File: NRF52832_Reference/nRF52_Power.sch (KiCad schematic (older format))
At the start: 32 parts

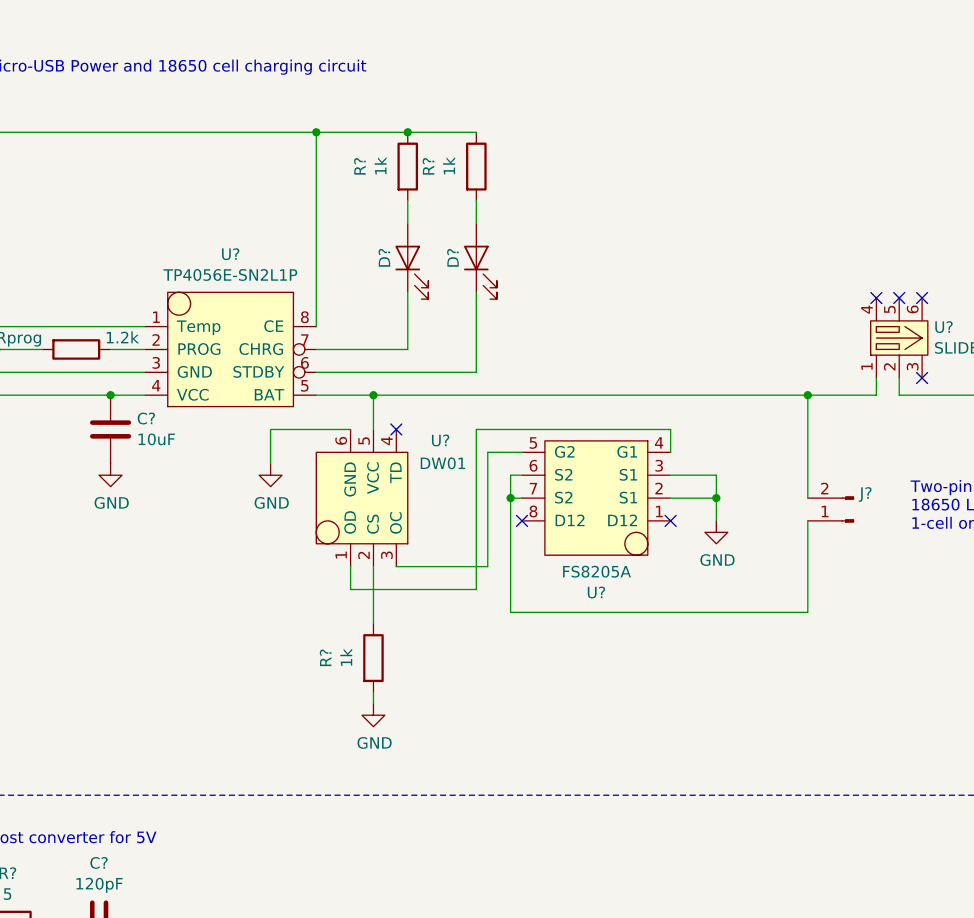
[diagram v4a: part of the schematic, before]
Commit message: Set footprints for some components of battery charging circuit.
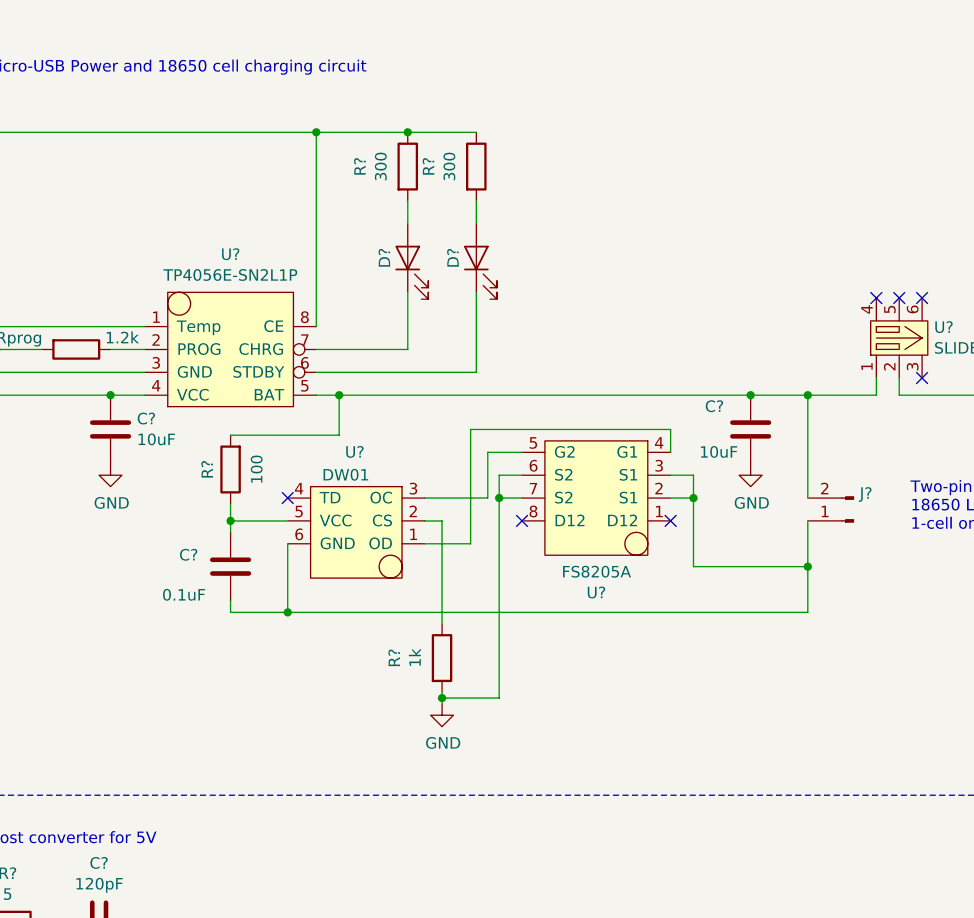
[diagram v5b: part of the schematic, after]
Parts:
- added C?: 10uF, Capacitor_SMD:C_0603_1608Metric_Pad1.05x0.95mm_HandSolder, symbol Device:C
- added C?: 0.1uF, Capacitor_SMD:C_0603_1608Metric_Pad1.05x0.95mm_HandSolder, symbol Device:C
- added R?: 100, Resistor_SMD:R_0603_1608Metric_Pad1.05x0.95mm_HandSolder, symbol Device:R
- C?: footprint (none) -> Capacitor_SMD:C_0603_1608Metric_Pad1.05x0.95mm_HandSolder
- D? (x2): footprint (none) -> LED_SMD:LED_0603_1608Metric_Pad1.05x0.95mm_HandSolder
- R? (x2): value 1k -> 300; footprint (none) -> Resistor_SMD:R_0603_1608Metric_Pad1.05x0.95mm_HandSolder
- R? (x5), Rprog: footprint (none) -> Resistor_SMD:R_0603_1608Metric_Pad1.05x0.95mm_HandSolder
- U?: footprint (none) -> Package_SO:SOIC-8-1EP_3.9x4.9mm_P1.27mm_EP2.35x2.35mm
- U?: footprint (none) -> Package_TO_SOT_SMD:SOT-23-6_Handsoldering
- U?: footprint (none) -> Package_SO:TSSOP-8_4.4x3mm_P0.65mm
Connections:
- net GND: now also U?.6 (S2), U?.7 (S2), C?.2; no longer U?.2 (S1), U?.3 (S1), U?.6 (GND)
- net at J?.2 (Pin_2), U?.1, U?.5 (BAT): now also C?.1, R?.2; no longer U?.5 (VCC)
- new net: C?.2, J?.1 (Pin_1), U?.2 (S1), U?.3 (S1), U?.6 (GND)
- new net: C?.1, R?.1, U?.5 (VCC)
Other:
- moved on the sheet: R?, U?
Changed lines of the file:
@@
 F 0 "D?" H 3850 1650 50  0000 C CNN
 F 1 "LED" H 3841 1675 50  0001 C CNN
-F 2 "" H 3850 1550 50  0001 C CNN
+F 2 "LED_SMD:LED_0603_1608Metric_Pad1.05x0.95mm_HandSolder" H 3850 1550 50  0001 C CNN
 F 3 "~" H 3850 1550 50  0001 C CNN
 	1    3850 1550
@@
 F 0 "D?" H 3550 1650 50  0000 C CNN
 F 1 "LED" H 3541 1675 50  0001 C CNN
-F 2 "" H 3550 1550 50  0001 C CNN
+F 2 "LED_SMD:LED_0603_1608Metric_Pad1.05x0.95mm_HandSolder" H 3550 1550 50  0001 C CNN
 F 3 "~" H 3550 1550 50  0001 C CNN
 	1    3550 1550
@@
 P 3850 1150
 F 0 "R?" V 3643 1150 50  0000 C CNN
-F 1 "1k" V 3734 1150 50  0000 C CNN
-F 2 "" V 3780 1150 50  0001 C CNN
+F 1 "300" V 3734 1150 50  0000 C CNN
+F 2 "Resistor_SMD:R_0603_1608Metric_Pad1.05x0.95mm_HandSolder" V 3780 1150 50  0001 C CNN
 F 3 "~" H 3850 1150 50  0001 C CNN
 	1    3850 1150
@@
 P 3550 1150
 F 0 "R?" V 3343 1150 50  0000 C CNN
-F 1 "1k" V 3434 1150 50  0000 C CNN
-F 2 "" V 3480 1150 50  0001 C CNN
+F 1 "300" V 3434 1150 50  0000 C CNN
+F 2 "Resistor_SMD:R_0603_1608Metric_Pad1.05x0.95mm_HandSolder" V 3480 1150 50  0001 C CNN
 F 3 "~" H 3550 1150 50  0001 C CNN
 	1    3550 1150
@@
 F 0 "U?" H 2775 2365 50  0000 C CNN
 F 1 "TP4056E-SN2L1P" H 2775 2274 50  0000 C CNN
-F 2 "" H 2650 1950 50  0001 C CNN
+F 2 "Package_SO:SOIC-8-1EP_3.9x4.9mm_P1.27mm_EP2.35x2.35mm" H 2650 1950 50  0001 C CNN
 F 3 "" H 2650 1950 50  0001 C CNN
 	1    2650 1950
 	1    0    0    -1
-$EndComp
-$Comp
-L Project_Libary:DW01 U?
-U 1 1 5BF3803F
-P 3450 2650
-F 0 "U?" V 3750 2450 50  0000 R CNN
-F 1 "DW01" V 3650 2500 50  0000 R CNN
-F 2 "" H 3450 2650 50  0001 C CNN
-F 3 "" H 3450 2650 50  0001 C CNN
-	1    3450 2650
-	0    -1   -1   0
 $EndComp
 $Comp
@@
 F 0 "U?" H 4425 3015 50  0000 C CNN
 F 1 "FS8205A" H 4425 2924 50  0000 C CNN
-F 2 "" H 4450 2950 50  0001 C CNN
+F 2 "Package_SO:TSSOP-8_4.4x3mm_P0.65mm" H 4450 2950 50  0001 C CNN
 F 3 "" H 4450 2950 50  0001 C CNN
 	1    4400 2650
@@
 F 0 "Rprog" V 2050 1700 50  0000 C CNN
 F 1 "1.2k" V 2050 2150 50  0000 C CNN
-F 2 "" V 2030 1950 50  0001 C CNN
+F 2 "Resistor_SMD:R_0603_1608Metric_Pad1.05x0.95mm_HandSolder" V 2030 1950 50  0001 C CNN
 F 3 "~" H 2100 1950 50  0001 C CNN
 	1    2100 1950
@@
 Wire Wire Line
 	3850 2050 3850 1700
-NoConn ~ 3500 2300
-Wire Wire Line
-	3400 2150 3400 2300
-$Comp
-L power:GND #PWR?
-U 1 1 5BF3E673
-P 2950 2450
-F 0 "#PWR?" H 2950 2200 50  0001 C CNN
-F 1 "GND" H 2955 2277 50  0000 C CNN
-F 2 "" H 2950 2450 50  0001 C CNN
-F 3 "" H 2950 2450 50  0001 C CNN
-	1    2950 2450
-	1    0    0    -1
-$EndComp
-Wire Wire Line
-	3300 2300 2950 2300
-Wire Wire Line
-	2950 2300 2950 2450
+NoConn ~ 3025 2600
 Wire Wire Line
 	1550 2150 1550 1000
@@
 F 0 "C?" H 2365 2346 50  0000 L CNN
 F 1 "10uF" H 2365 2255 50  0000 L CNN
-F 2 "" H 2288 2150 50  0001 C CNN
+F 2 "Capacitor_SMD:C_0603_1608Metric_Pad1.05x0.95mm_HandSolder" H 2288 2150 50  0001 C CNN
 F 3 "~" H 2250 2300 50  0001 C CNN
 	1    2250 2300
@@
 L Device:R R?
 U 1 1 5BF44C1F
-P 3400 3300
-F 0 "R?" V 3193 3300 50  0000 C CNN
-F 1 "1k" V 3284 3300 50  0000 C CNN
-F 2 "" V 3330 3300 50  0001 C CNN
-F 3 "~" H 3400 3300 50  0001 C CNN
-	1    3400 3300
+P 3700 3300
+F 0 "R?" V 3493 3300 50  0000 C CNN
+F 1 "1k" V 3584 3300 50  0000 C CNN
+F 2 "Resistor_SMD:R_0603_1608Metric_Pad1.05x0.95mm_HandSolder" V 3630 3300 50  0001 C CNN
+F 3 "~" H 3700 3300 50  0001 C CNN
+	1    3700 3300
 	1    0    0    -1
 $EndComp
@@
 L power:GND #PWR?
 U 1 1 5BF44FAE
-P 3400 3500
-F 0 "#PWR?" H 3400 3250 50  0001 C CNN
-F 1 "GND" H 3405 3327 50  0000 C CNN
-F 2 "" H 3400 3500 50  0001 C CNN
-F 3 "" H 3400 3500 50  0001 C CNN
-	1    3400 3500
-	1    0    0    -1
-$EndComp
-Wire Wire Line
-	3500 2900 3900 2900
-Wire Wire Line
-	3900 2900 3900 2400
+P 3700 3500
+F 0 "#PWR?" H 3700 3250 50  0001 C CNN
+F 1 "GND" H 3705 3327 50  0000 C CNN
+F 2 "" H 3700 3500 50  0001 C CNN
+F 3 "" H 3700 3500 50  0001 C CNN
+	1    3700 3500
+	1    0    0    -1
+$EndComp
 Wire Wire Line
 	3900 2400 4050 2400
 Wire Wire Line
-	3400 2900 3400 3150
-Wire Wire Line
-	3400 3450 3400 3500
-Wire Wire Line
-	3300 3000 3850 3000
-Wire Wire Line
-	3850 3000 3850 2300
-Wire Wire Line
-	3850 2300 4700 2300
-Wire Wire Line
 	4700 2300 4700 2400
-Wire Wire Line
-	3300 2900 3300 3000
 $Comp
 L power:GND #PWR?
 U 1 1 5BF49B8A
-P 4900 2700
-F 0 "#PWR?" H 4900 2450 50  0001 C CNN
-F 1 "GND" H 4905 2527 50  0000 C CNN
-F 2 "" H 4900 2700 50  0001 C CNN
-F 3 "" H 4900 2700 50  0001 C CNN
-	1    4900 2700
-	1    0    0    -1
-$EndComp
-Wire Wire Line
-	4700 2600 4900 2600
-Wire Wire Line
-	4900 2600 4900 2700
-Wire Wire Line
-	4700 2500 4900 2500
-Wire Wire Line
-	4900 2500 4900 2600
-Connection ~ 4900 2600
-Wire Wire Line
-	4050 2500 4000 2500
-Wire Wire Line
-	4000 2500 4000 2600
-Wire Wire Line
-	4000 3100 5300 3100
-Wire Wire Line
-	5300 3100 5300 2700
+P 5050 2450
+F 0 "#PWR?" H 5050 2200 50  0001 C CNN
+F 1 "GND" H 5055 2277 50  0000 C CNN
+F 2 "" H 5050 2450 50  0001 C CNN
+F 3 "" H 5050 2450 50  0001 C CNN
+	1    5050 2450
+	1    0    0    -1
+$EndComp
 Wire Wire Line
 	5300 2600 5300 2150
-Wire Wire Line
-	5300 2150 3400 2150
-Connection ~ 3400 2150
-Wire Wire Line
-	3400 2150 3150 2150
-Wire Wire Line
-	4050 2600 4000 2600
-Connection ~ 4000 2600
-Wire Wire Line
-	4000 2600 4000 3100
 NoConn ~ 4050 2700
 NoConn ~ 4700 2700
@@
 F 0 "R?" V 1593 4450 50  0000 C CNN
 F 1 "5" V 1684 4450 50  0000 C CNN
-F 2 "" V 1730 4450 50  0001 C CNN
+F 2 "Resistor_SMD:R_0603_1608Metric_Pad1.05x0.95mm_HandSolder" V 1730 4450 50  0001 C CNN
 F 3 "~" H 1800 4450 50  0001 C CNN
 	1    1800 4450
@@
 F 0 "R?" H 3220 5296 50  0000 L CNN
 F 1 "100k" H 3220 5205 50  0000 L CNN
-F 2 "" V 3080 5250 50  0001 C CNN
+F 2 "Resistor_SMD:R_0603_1608Metric_Pad1.05x0.95mm_HandSolder" V 3080 5250 50  0001 C CNN
 F 3 "~" H 3150 5250 50  0001 C CNN
 	1    3150 5250
@@
 F 0 "R?" H 3000 5800 50  0000 L CNN
 F 1 "220k" H 2900 5700 50  0000 L CNN
-F 2 "" V 3080 5750 50  0001 C CNN
+F 2 "Resistor_SMD:R_0603_1608Metric_Pad1.05x0.95mm_HandSolder" V 3080 5750 50  0001 C CNN
 F 3 "~" H 3150 5750 50  0001 C CNN
 	1    3150 5750
@@
 F 0 "R?" H 4650 5500 50  0000 L CNN
 F 1 "220" H 4600 5375 50  0000 L CNN
-F 2 "" V 4730 5400 50  0001 C CNN
+F 2 "Resistor_SMD:R_0603_1608Metric_Pad1.05x0.95mm_HandSolder" V 4730 5400 50  0001 C CNN
 F 3 "~" H 4800 5400 50  0001 C CNN
 	1    4800 5400
@@
 Wire Wire Line
 	1075 6500 3325 6500
+$Comp
+L Device:C C?
+U 1 1 5C0D1C4A
+P 5050 2300
+F 0 "C?" H 4850 2400 50  0000 L CNN
+F 1 "10uF" H 4825 2200 50  0000 L CNN
+F 2 "Capacitor_SMD:C_0603_1608Metric_Pad1.05x0.95mm_HandSolder" H 5088 2150 50  0001 C CNN
+F 3 "~" H 5050 2300 50  0001 C CNN
+	1    5050 2300
+	1    0    0    -1
+$EndComp
+Connection ~ 5050 2150
+Wire Wire Line
+	5050 2150 5300 2150
+Wire Wire Line
+	4050 2500 3950 2500
+Wire Wire Line
+	3950 2500 3950 2600
+$Comp
+L Project_Libary:DW01 U?
+U 1 1 5BF3803F
+P 3375 2650
+F 0 "U?" H 3475 2400 50  0000 R CNN
+F 1 "DW01" H 3575 2500 50  0000 R CNN
+F 2 "Package_TO_SOT_SMD:SOT-23-6_Handsoldering" H 3375 2650 50  0001 C CNN
+F 3 "" H 3375 2650 50  0001 C CNN
+	1    3375 2650
+	-1   0    0    1
+$EndComp
+Wire Wire Line
+	3950 2600 4050 2600
+Connection ~ 3950 2600
+Wire Wire Line
+	3950 2600 3950 3475
+Wire Wire Line
+	4700 2600 4800 2600
+Wire Wire Line
+	4800 2600 4800 2900
+Wire Wire Line
+	4800 2900 5300 2900
+Wire Wire Line
+	5300 2900 5300 2700
+Wire Wire Line
+	4700 2500 4800 2500
+Wire Wire Line
+	4800 2500 4800 2600
+Connection ~ 4800 2600
+Wire Wire Line
+	3150 2150 3250 2150
+Wire Wire Line
+	3625 2600 3900 2600
+Wire Wire Line
+	3900 2600 3900 2400
+Wire Wire Line
+	3625 2800 3825 2800
+Wire Wire Line
+	3825 2800 3825 2300
+Wire Wire Line
+	3825 2300 4700 2300
+Wire Wire Line
+	3700 3450 3700 3475
+Wire Wire Line
+	3625 2700 3700 2700
+Wire Wire Line
+	3700 2700 3700 3150
+Wire Wire Line
+	3950 3475 3700 3475
+Connection ~ 3700 3475
+Wire Wire Line
+	3700 3475 3700 3500
+$Comp
+L Device:R R?
+U 1 1 5C116645
+P 2775 2475
+F 0 "R?" V 2875 2475 50  0000 C CNN
+F 1 "100" V 2659 2475 50  0000 C CNN
+F 2 "Resistor_SMD:R_0603_1608Metric_Pad1.05x0.95mm_HandSolder" V 2705 2475 50  0001 C CNN
+F 3 "~" H 2775 2475 50  0001 C CNN
+	1    2775 2475
+	-1   0    0    1
+$EndComp
+$Comp
+L Device:C C?
+U 1 1 5C116A5B
+P 2775 2900
+F 0 "C?" H 2550 2950 50  0000 L CNN
+F 1 "0.1uF" H 2475 2775 50  0000 L CNN
+F 2 "Capacitor_SMD:C_0603_1608Metric_Pad1.05x0.95mm_HandSolder" H 2813 2750 50  0001 C CNN
+F 3 "~" H 2775 2900 50  0001 C CNN
+	1    2775 2900
+	1    0    0    -1
+$EndComp
+Wire Wire Line
+	2775 2325 3250 2325
+Wire Wire Line
+	3250 2325 3250 2150
+Connection ~ 3250 2150
+Wire Wire Line
+	3250 2150 5050 2150
+Wire Wire Line
+	3025 2700 2775 2700
+Wire Wire Line
+	2775 2625 2775 2700
+Connection ~ 2775 2700
+Wire Wire Line
+	2775 2700 2775 2750
+Wire Wire Line
+	2775 3050 2775 3100
+Wire Wire Line
+	2775 3100 3025 3100
+Wire Wire Line
+	5300 3100 5300 2900
+Connection ~ 5300 2900
+Wire Wire Line
+	3025 2800 3025 3100
+Connection ~ 3025 3100
+Wire Wire Line
+	3025 3100 5300 3100
 $EndSCHEMATC

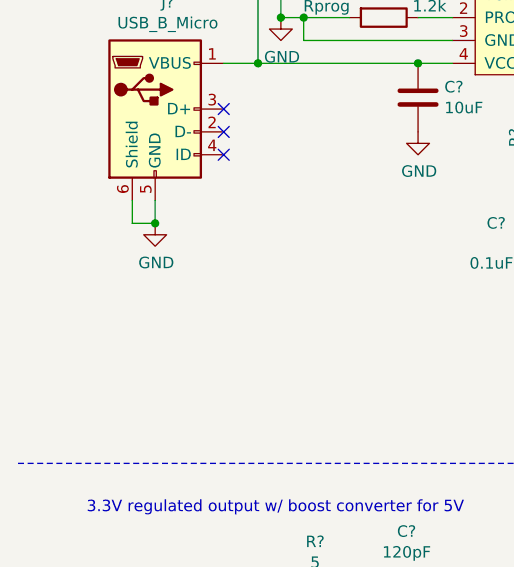
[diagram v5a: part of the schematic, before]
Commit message: Added Micro USB type B footprint
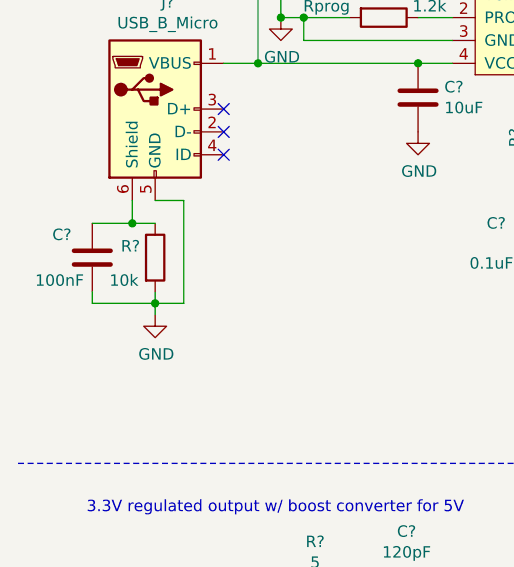
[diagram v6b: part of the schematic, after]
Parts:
- added C?: 100nF, Capacitor_SMD:C_0603_1608Metric_Pad1.05x0.95mm_HandSolder, symbol Device:C
- added R?: 10k, Resistor_SMD:R_0603_1608Metric_Pad1.05x0.95mm_HandSolder, symbol Device:R
- J?: footprint (none) -> Custom_Footprints:USB_Micro_B_Amphenol_10118194-0001LF
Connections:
- net GND: now also C?.2, R?.2; no longer J?.6 (Shield)
- new net: C?.1, J?.6 (Shield), R?.1
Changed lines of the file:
@@
 F 0 "J?" H 1155 2817 50  0000 C CNN
 F 1 "USB_B_Micro" H 1155 2726 50  0000 C CNN
-F 2 "" H 1250 2300 50  0001 C CNN
+F 2 "Custom_Footprints:USB_Micro_B_Amphenol_10118194-0001LF" H 1250 2300 50  0001 C CNN
 F 3 "~" H 1250 2300 50  0001 C CNN
 	1    1100 2350
@@
 L power:GND #PWR?
 U 1 1 5BF34114
-P 1100 2850
-F 0 "#PWR?" H 1100 2600 50  0001 C CNN
-F 1 "GND" H 1105 2677 50  0000 C CNN
-F 2 "" H 1100 2850 50  0001 C CNN
-F 3 "" H 1100 2850 50  0001 C CNN
-	1    1100 2850
+P 1100 3250
+F 0 "#PWR?" H 1100 3000 50  0001 C CNN
+F 1 "GND" H 1105 3077 50  0000 C CNN
+F 2 "" H 1100 3250 50  0001 C CNN
+F 3 "" H 1100 3250 50  0001 C CNN
+	1    1100 3250
 	1    0    0    -1
 $EndComp
 Wire Wire Line
 	1000 2750 1000 2850
-Wire Wire Line
-	1000 2850 1100 2850
-Wire Wire Line
-	1100 2750 1100 2850
-Connection ~ 1100 2850
 $Comp
 L Device:R R?
@@
 Wire Wire Line
 	3025 3100 5300 3100
+$Comp
+L Device:R R?
+U 1 1 5C0E61D3
+P 1100 3000
+F 0 "R?" H 950 3050 50  0000 L CNN
+F 1 "10k" H 900 2900 50  0000 L CNN
+F 2 "Resistor_SMD:R_0603_1608Metric_Pad1.05x0.95mm_HandSolder" V 1030 3000 50  0001 C CNN
+F 3 "~" H 1100 3000 50  0001 C CNN
+	1    1100 3000
+	1    0    0    -1
+$EndComp
+$Comp
+L Device:C C?
+U 1 1 5C0E63EC
+P 825 3000
+F 0 "C?" H 650 3100 50  0000 L CNN
+F 1 "100nF" H 575 2900 50  0000 L CNN
+F 2 "Capacitor_SMD:C_0603_1608Metric_Pad1.05x0.95mm_HandSolder" H 863 2850 50  0001 C CNN
+F 3 "~" H 825 3000 50  0001 C CNN
+	1    825  3000
+	1    0    0    -1
+$EndComp
+Wire Wire Line
+	1100 2850 1000 2850
+Connection ~ 1000 2850
+Wire Wire Line
+	1000 2850 825  2850
+Wire Wire Line
+	1100 2750 1225 2750
+Wire Wire Line
+	1225 2750 1225 3200
+Wire Wire Line
+	1225 3200 1100 3200
+Wire Wire Line
+	1100 3200 1100 3250
+Wire Wire Line
+	1100 3150 1100 3200
+Connection ~ 1100 3200
+Wire Wire Line
+	825  3150 825  3200
+Wire Wire Line
+	825  3200 1100 3200
 $EndSCHEMATC

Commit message: Added SW_DPDT_Slide footprint. Finished updating footprints for all USB/Battery charger components.
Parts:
- C? (x8): footprint (none) -> Capacitor_SMD:C_0603_1608Metric_Pad1.05x0.95mm_HandSolder
- D?: footprint (none) -> LED_SMD:LED_0603_1608Metric_Pad1.05x0.95mm_HandSolder
- J?: footprint (none) -> Connector_PinHeader_2.54mm:PinHeader_1x02_P2.54mm_Horizontal
- U?: footprint (none) -> Custom_Footprints:SW_DPDT_Slide_JS202011CQN
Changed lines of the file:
@@
 F 0 "J?" H 5473 2580 50  0000 R CNN
 F 1 "Conn_01x02_Male" H 5473 2671 50  0001 R CNN
-F 2 "" H 5500 2700 50  0001 C CNN
+F 2 "Connector_PinHeader_2.54mm:PinHeader_1x02_P2.54mm_Horizontal" H 5500 2700 50  0001 C CNN
 F 3 "~" H 5500 2700 50  0001 C CNN
 	1    5500 2700
@@
 F 0 "C?" H 1250 7125 50  0000 L CNN
 F 1 "4.7uF" H 1175 7000 50  0000 L CNN
-F 2 "" H 1538 6925 50  0001 C CNN
+F 2 "Capacitor_SMD:C_0603_1608Metric_Pad1.05x0.95mm_HandSolder" H 1538 6925 50  0001 C CNN
 F 3 "~" H 1500 7075 50  0001 C CNN
 	1    1500 7075
@@
 F 0 "C?" H 2050 5300 50  0000 L CNN
 F 1 "10uF" H 2050 5150 50  0000 L CNN
-F 2 "" H 2313 5100 50  0001 C CNN
+F 2 "Capacitor_SMD:C_0603_1608Metric_Pad1.05x0.95mm_HandSolder" H 2313 5100 50  0001 C CNN
 F 3 "~" H 2275 5250 50  0001 C CNN
 	1    2275 5250
@@
 F 0 "C?" V 1948 4450 50  0000 C CNN
 F 1 "120pF" V 2039 4450 50  0000 C CNN
-F 2 "" H 2238 4300 50  0001 C CNN
+F 2 "Capacitor_SMD:C_0603_1608Metric_Pad1.05x0.95mm_HandSolder" H 2238 4300 50  0001 C CNN
 F 3 "~" H 2200 4450 50  0001 C CNN
 	1    2200 4450
@@
 F 0 "C?" H 2475 7150 50  0000 L CNN
 F 1 "4.7uF" H 2440 7030 50  0000 L CNN
-F 2 "" H 2363 6925 50  0001 C CNN
+F 2 "Capacitor_SMD:C_0603_1608Metric_Pad1.05x0.95mm_HandSolder" H 2363 6925 50  0001 C CNN
 F 3 "~" H 2325 7075 50  0001 C CNN
 	1    2325 7075
@@
 F 0 "D?" H 4641 5966 50  0000 C CNN
 F 1 "LED" H 4641 5875 50  0000 C CNN
-F 2 "" H 4650 5750 50  0001 C CNN
+F 2 "LED_SMD:LED_0603_1608Metric_Pad1.05x0.95mm_HandSolder" H 4650 5750 50  0001 C CNN
 F 3 "~" H 4650 5750 50  0001 C CNN
 	1    4650 5750
@@
 F 0 "C?" H 2425 5325 50  0000 L CNN
 F 1 "10uF" H 2425 5150 50  0000 L CNN
-F 2 "" H 2663 5100 50  0001 C CNN
+F 2 "Capacitor_SMD:C_0603_1608Metric_Pad1.05x0.95mm_HandSolder" H 2663 5100 50  0001 C CNN
 F 3 "~" H 2625 5250 50  0001 C CNN
 	1    2625 5250
@@
 F 0 "C?" H 2750 5325 50  0000 L CNN
 F 1 "10uF" H 2750 5150 50  0000 L CNN
-F 2 "" H 2988 5100 50  0001 C CNN
+F 2 "Capacitor_SMD:C_0603_1608Metric_Pad1.05x0.95mm_HandSolder" H 2988 5100 50  0001 C CNN
 F 3 "~" H 2950 5250 50  0001 C CNN
 	1    2950 5250
@@
 F 0 "C?" H 4625 7125 50  0000 L CNN
 F 1 "4.7uF" H 4590 7005 50  0000 L CNN
-F 2 "" H 4513 6900 50  0001 C CNN
+F 2 "Capacitor_SMD:C_0603_1608Metric_Pad1.05x0.95mm_HandSolder" H 4513 6900 50  0001 C CNN
 F 3 "~" H 4475 7050 50  0001 C CNN
 	1    4475 7050
@@
 F 0 "C?" H 3640 7096 50  0000 L CNN
 F 1 "1uF" H 3640 7005 50  0000 L CNN
-F 2 "" H 3563 6900 50  0001 C CNN
+F 2 "Capacitor_SMD:C_0603_1608Metric_Pad1.05x0.95mm_HandSolder" H 3563 6900 50  0001 C CNN
 F 3 "~" H 3525 7050 50  0001 C CNN
 	1    3525 7050
@@
 F 0 "U?" H 5852 1946 50  0000 L CNN
 F 1 "SLIDE_SW_DPDT" H 5852 1855 50  0000 L CNN
-F 2 "" H 5700 2150 50  0001 C CNN
+F 2 "Custom_Footprints:SW_DPDT_Slide_JS202011CQN" H 5700 2150 50  0001 C CNN
 F 3 "" H 5700 2150 50  0001 C CNN
 	1    5700 1900
